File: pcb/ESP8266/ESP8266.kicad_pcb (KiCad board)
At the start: 2 copper layers, 17.5 x 27.2 mm, 18 parts, among them J1 Conn_02x04, U1 ESP8266EX, U2 W25Q16BVSSIG

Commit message: mejoras en el pcb
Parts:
- J1: footprint Connector_PinHeader_1.27mm:PinHeader_2x04_P1.27mm_Vertical -> Connector_PinHeader_2.54mm:PinHeader_2x04_P2.54mm_Vertical
- moved J1 0.79 mm to (107.0, 136.0)
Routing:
- net /RST: track 31.9 -> 18.6 mm
- net /UTXD: track 44.2 -> 32.7 mm
- net /GPIO2: track 8.27 -> 12.4 mm, vias 1 -> 2
- net /URXD: track 22.9 -> 19.3 mm
- net +3V3: track 60.6 -> 63.9 mm
- net /ENA: track 13.6 -> 12.1 mm, vias 2 -> 0
- net /GPIO0: track 5.71 -> 6.39 mm, vias 0 -> 1
- net GND: track 128.9 -> 128.4 mm

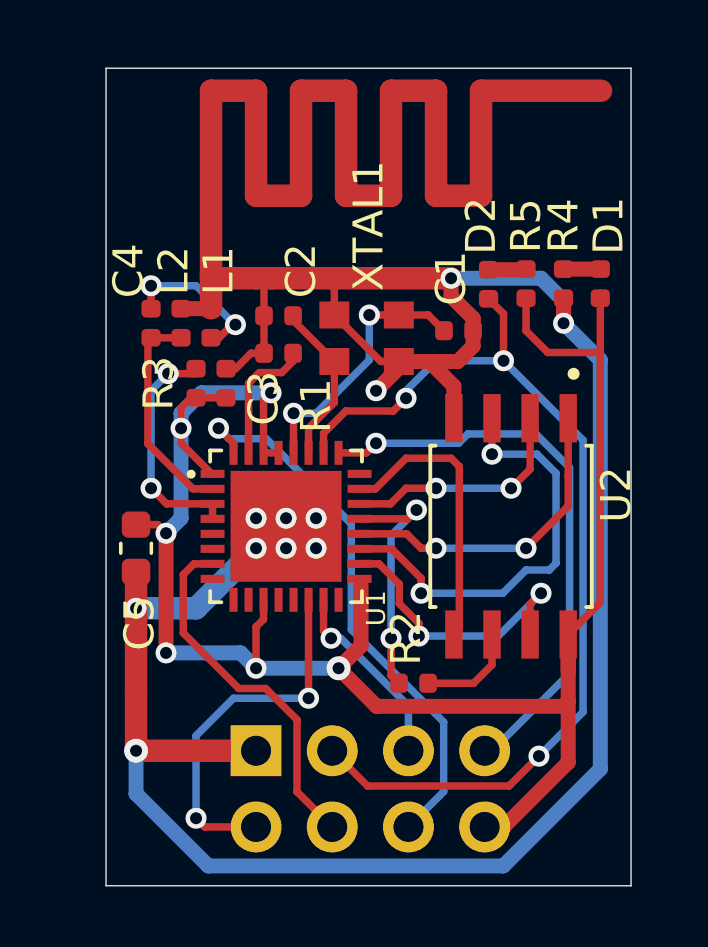
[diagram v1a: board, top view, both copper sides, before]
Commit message: agregado de modelos 3D al proeycto, fiduciales y agujero
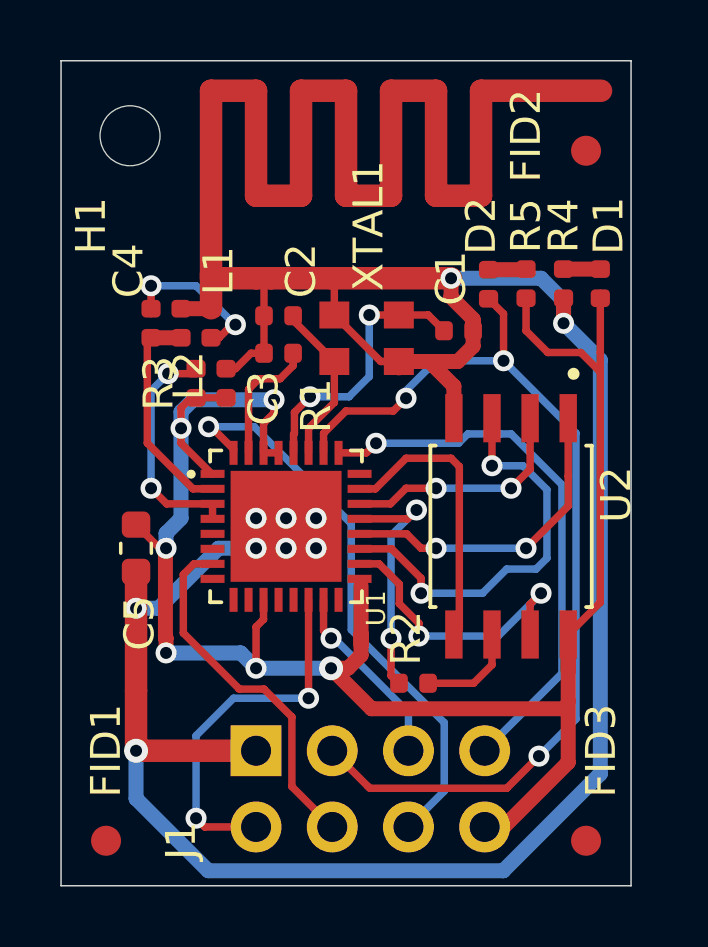
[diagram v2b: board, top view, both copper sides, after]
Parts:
- added FID1: Fiducial, Fiducial:Fiducial_1mm_Mask2mm, F.Cu at (102.0, 139.0)
- added FID2: Fiducial, Fiducial:Fiducial_1mm_Mask2mm, F.Cu at (118.0, 116.0)
- added FID3: Fiducial, Fiducial:Fiducial_1mm_Mask2mm, F.Cu at (118.0, 139.0)
- added H1: MountingHole, MountingHole:MountingHole_2mm, F.Cu at (102.8, 115.5)
- turned L2 to 270 degrees
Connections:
- L2 pad 1: Net-(C4-Pad1) -> GND
- L2 pad 2: GND -> Net-(C4-Pad1)
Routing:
- net +3V3: track 63.9 -> 65.0 mm
- net /URXD: track 19.3 -> 18.3 mm
- net Net-(U1-Pad19): track 14.5 -> 13.7 mm
- net /RST: track 18.6 -> 19.2 mm
- net GND: track 128.4 -> 128.1 mm, vias 11 -> 10
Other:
- board size 17.5 x 27.2 mm -> 19 x 27.5 mm
- net class Default: clearance 0.2 -> 0.22
- rule trace_clearance: 0.2 -> 0.22

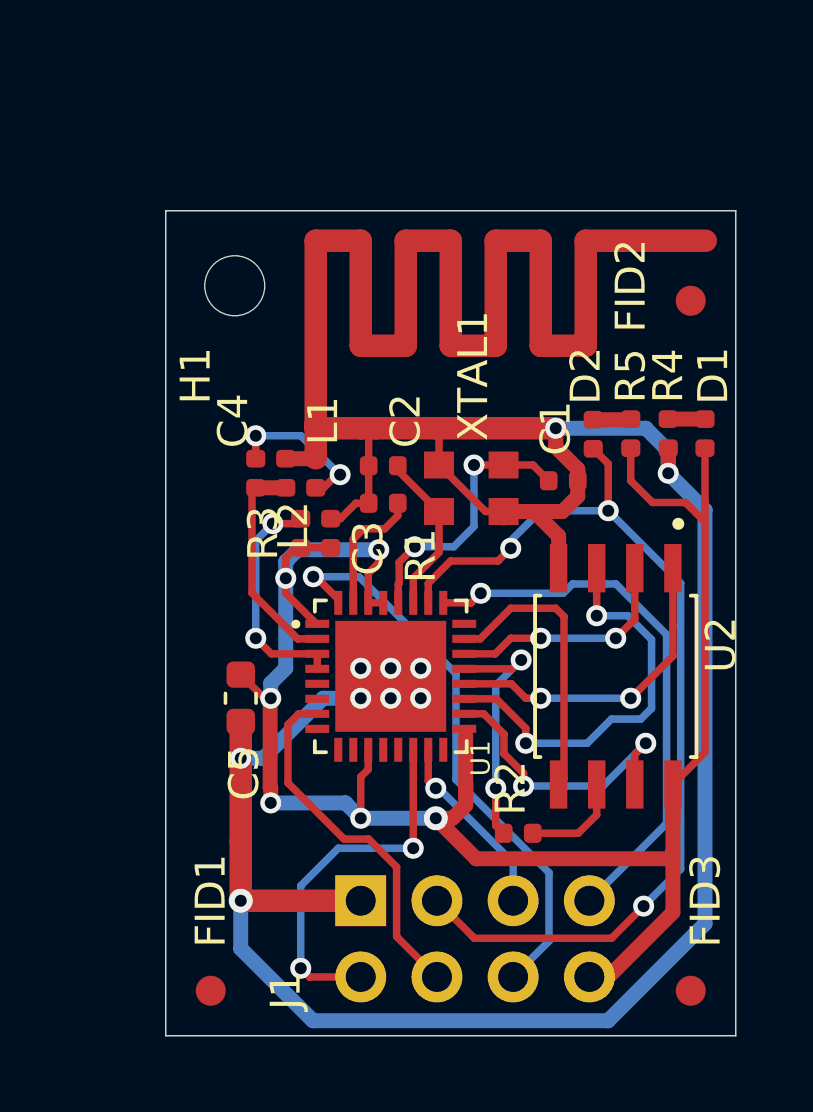
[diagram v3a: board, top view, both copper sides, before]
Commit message: board acomodado con componentes 0805
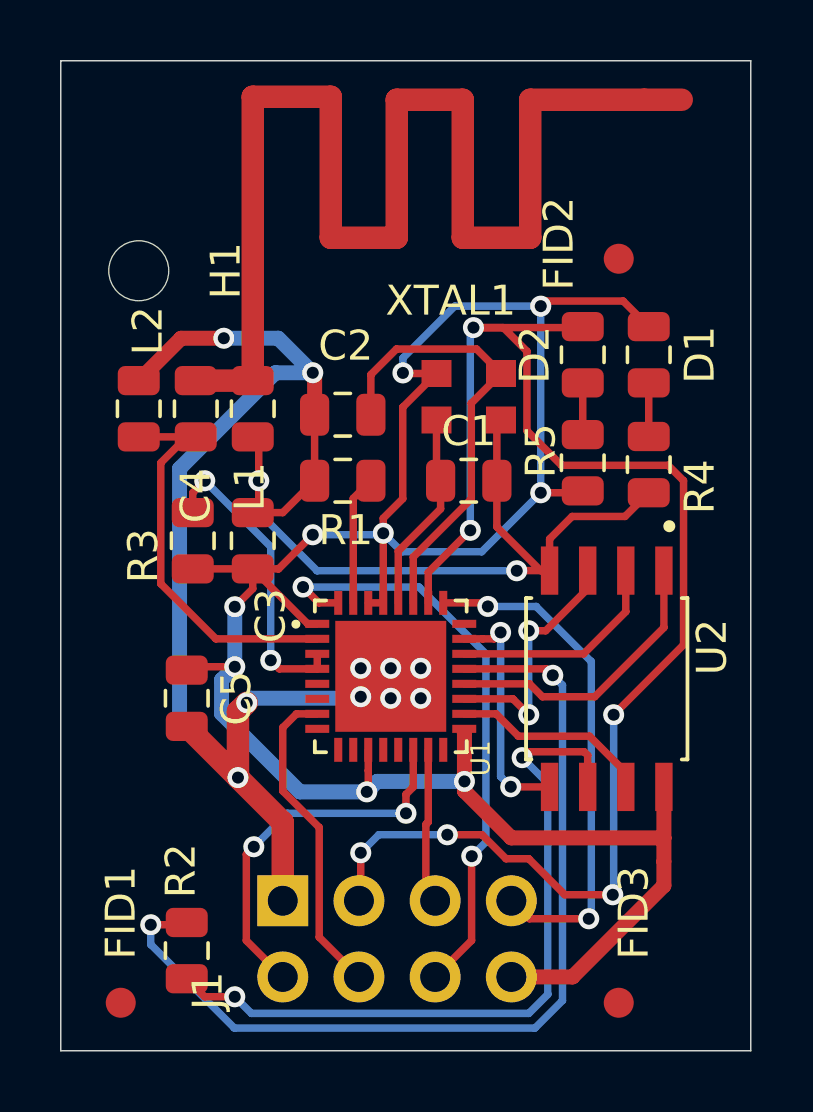
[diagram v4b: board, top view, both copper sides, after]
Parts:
- C1, C2, C3, C4: footprint Capacitor_SMD:C_0402_1005Metric -> Capacitor_SMD:C_0805_2012Metric
- C5: footprint Capacitor_SMD:C_0603_1608Metric -> Capacitor_SMD:C_0805_2012Metric
- D1, D2, R1, R2, R3, R4, R5: footprint Resistor_SMD:R_0402_1005Metric -> Resistor_SMD:R_0805_2012Metric
- L1, L2: footprint Inductor_SMD:L_0402_1005Metric -> Inductor_SMD:L_0805_2012Metric
- moved R2 11.7 mm to (101.2, 137.7), turned to 90 degrees
- moved L2 5.35 mm to (99.6, 119.6)
- moved R3 3.61 mm to (101.4, 124.0)
- moved H1 3.24 mm to (99.6, 115.0)
- moved D1 3.23 mm to (116.6, 117.8), turned to 90 degrees
- moved C1 3.15 mm to (110.6, 122.0)
- moved XTAL1 3.05 mm to (110.6, 119.2), turned to 0 degrees
- moved FID1 3.03 mm to (99.0, 139.4)
- moved L1 3.01 mm to (103.4, 119.6), turned to 90 degrees
- moved C4 2.94 mm to (101.5, 119.6)
- moved FID2 2.78 mm to (115.6, 114.6)
- moved D2 2.67 mm to (114.4, 117.8), turned to 270 degrees
- moved C3 2.61 mm to (103.4, 124.0)
- moved J1 2.60 mm to (104.4, 136.0)
- moved FID3 2.43 mm to (115.6, 139.4)
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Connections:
- XTAL1 pad 4: GND -> +3V3
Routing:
- net GND: track 128.1 -> 74.7 mm, vias 10 -> 12
- net Net-(C4-Pad2): track 5.23 -> 44.2 mm, vias 2 -> 0
- net Net-(R2-Pad2): track 8.26 -> 31.3 mm
- net Net-(R2-Pad1): track 3.39 -> 24.4 mm, vias 0 -> 2
- net /UTXD: track 32.6 -> 50.0 mm, vias 3 -> 6
- net +3V3: track 65.0 -> 80.6 mm, vias 6 -> 9
- net /SA_XTAL: track 5.50 -> 15.2 mm
- net Net-(C4-Pad1): track 7.67 -> 13.1 mm
- net Net-(U1-Pad19): track 13.7 -> 8.32 mm
- net Net-(U1-Pad18): track 9.80 -> 6.68 mm, vias 2 -> 0
- net Net-(R3-Pad2): track 7.75 -> 10.3 mm
- net /EN_XTAL: track 9.11 -> 6.74 mm, vias 2 -> 0
- net Net-(U1-Pad23): track 9.54 -> 7.88 mm, vias 0 -> 2
- net /ENA: track 12.1 -> 10.7 mm
- net /URXD: track 18.3 -> 17.2 mm, vias 1 -> 2
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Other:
- board size 19 x 27.5 mm -> 23 x 33 mm
- net class Default: clearance 0.22 -> 0.24
- rule trace_clearance: 0.22 -> 0.24

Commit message: agregado de comentarios
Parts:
- moved FID3 53.4 mm to (157.0, 105.6)
- moved FID2 53.4 mm to (157.0, 80.8)
- moved U1 52.3 mm to (148.0, 94.8)
- moved C1 52.3 mm to (150.6, 88.2)
- moved C2 52.3 mm to (146.4, 86.0)
- moved C3 52.3 mm to (143.4, 90.2)
- moved C4 52.3 mm to (141.5, 85.8)
- moved D1 52.3 mm to (156.6, 84.0)
- moved D2 52.3 mm to (154.4, 84.0)
- moved FID1 52.3 mm to (139.0, 105.7)
- moved H1 52.3 mm to (139.6, 81.2)
- moved J1 52.3 mm to (144.4, 102.2)
- moved L1 52.3 mm to (143.4, 85.8)
- moved L2 52.3 mm to (139.6, 85.8)
- moved R1 52.3 mm to (146.4, 88.2)
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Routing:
- net Net-(C4-Pad2): track 44.2 -> 54.6 mm
- net /UTXD: track 50.0 -> 51.7 mm
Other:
- board text added: "* No se tiene restricciones sobre el tamaño de pistas. * Se utilizo las capacidades de fabricación nacional (Mayer). * La capacidad de Mayer planteada para este módulo fue 10 mils * La grilla utilizada para acomodar componente cómo primera aproximación fue 1mm * La grilla utilizada para routear las pistas varió entre 0.25 a 0.1mm"
- board text added: "ESP01 Rev 1.1 Ind Arg"

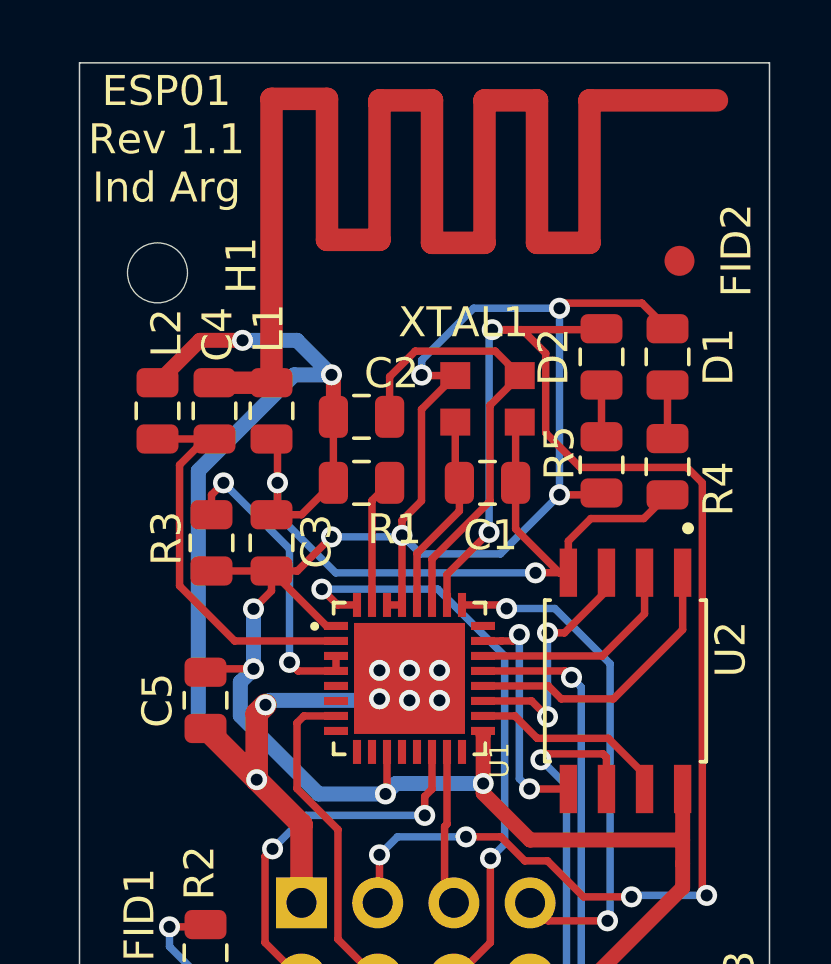
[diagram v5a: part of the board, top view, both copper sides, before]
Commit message: agregados componentes digikey
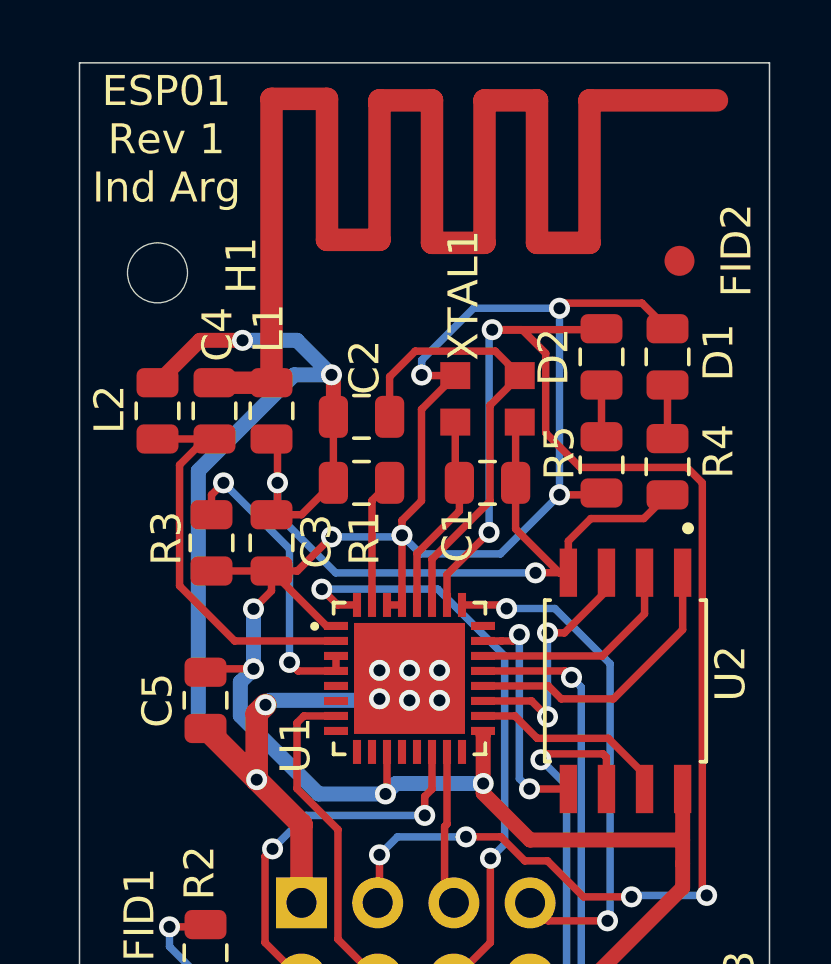
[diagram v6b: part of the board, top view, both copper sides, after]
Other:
- board text added: "ESP01 Rev 1 Ind Arg"
- board text removed: "ESP01 Rev 1.1 Ind Arg"

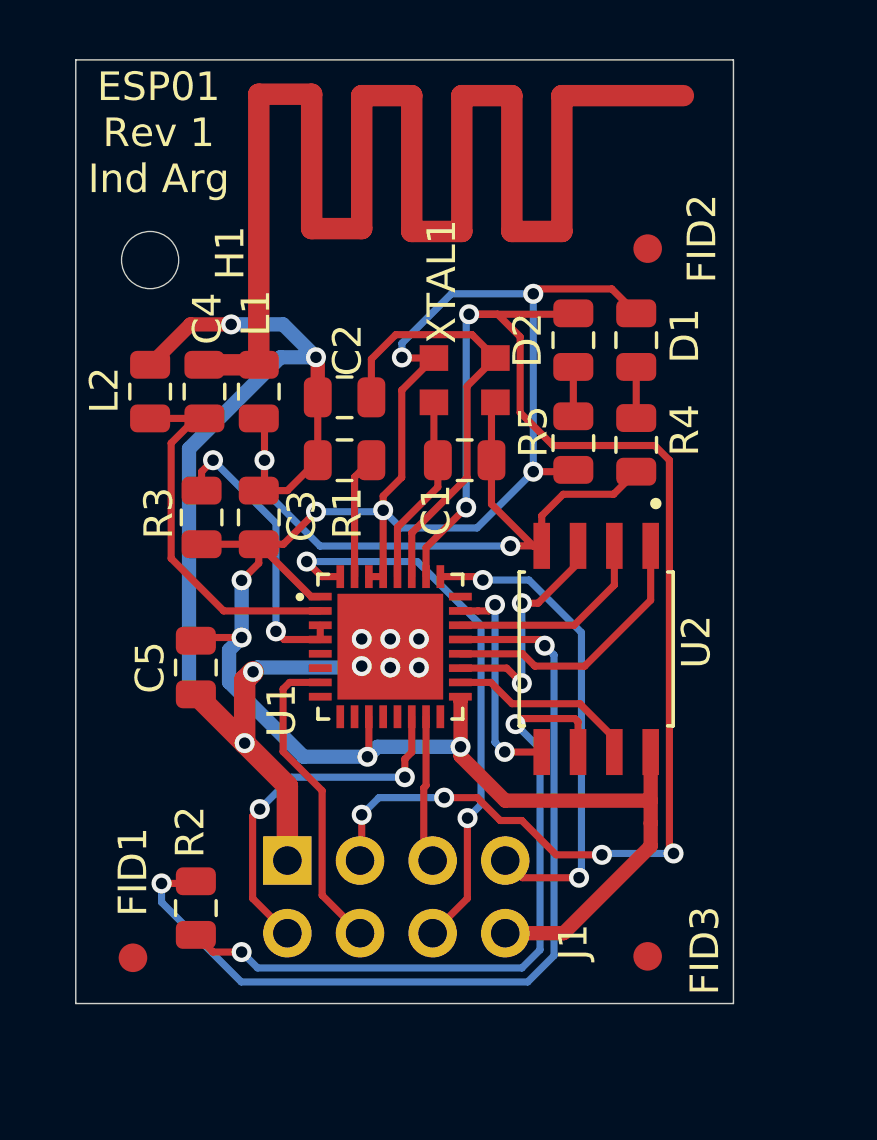
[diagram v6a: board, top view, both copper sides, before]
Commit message: agregado de logos y e informacion para fabricacion
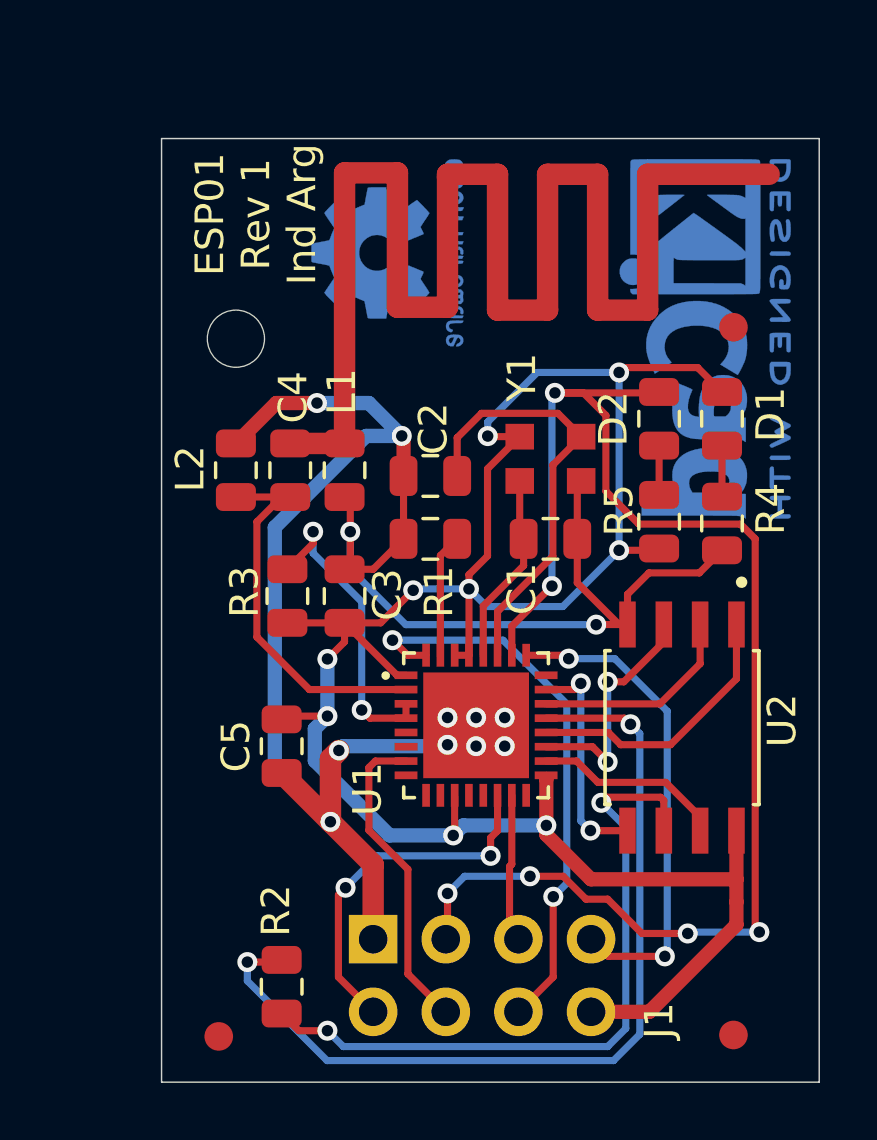
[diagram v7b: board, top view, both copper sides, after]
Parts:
- added LOGO1: Logo_Open_Hardware_Small, Symbol:KiCad-Logo2_5mm_Copper, B.Cu at (159.0, 84.0)
- added LOGO2: Logo_Open_Hardware_Small, Symbol:OSHW-Logo2_7.3x6mm_Copper, B.Cu at (148.0, 81.0)
- moved C1 4.07 mm to (153.6, 91.0)
- moved C2 4.07 mm to (149.4, 88.8)
- moved C3 4.07 mm to (146.4, 93.0)
- moved C4 4.07 mm to (144.5, 88.6)
- moved C5 4.07 mm to (144.2, 98.2)
- moved D1 4.07 mm to (159.6, 86.8)
- moved D2 4.07 mm to (157.4, 86.8)
- moved FID1 4.07 mm to (142.0, 108.4)
- moved FID2 4.07 mm to (160.0, 83.6)
- moved FID3 4.07 mm to (160.0, 108.3)
- moved H1 4.07 mm to (142.6, 84.0)
- moved J1 4.07 mm to (147.4, 105.0)
- moved L1 4.07 mm to (146.4, 88.6)
- moved L2 4.07 mm to (142.6, 88.6)
- moved R1 4.07 mm to (149.4, 91.0)
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- renumbered XTAL1 to Y1
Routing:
- net Net-(R3-Pad2): track 10.3 -> 10.8 mm
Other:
- board text added: "Board dimension: 23x33 mm 2 Layers - thickness: 1.6 mm Surface finish: HASL with lead Grid: 0.1mm Clearance: 0.24 mm Track Width: 0.25mm Via size: 0.7mm Via Drill: 0.4mm Tented Vias Reference specs: MAYER pcb"
- board text removed: "* No se tiene restricciones sobre el tamaño de pistas. * Se utilizo las capacidades de fabricación nacional (Mayer). * La capacidad de Mayer planteada para este módulo fue 10 mils * La grilla utilizada para acomodar componente cómo primera aproximación fue 1mm * La grilla utilizada para routear las pistas varió entre 0.25 a 0.1mm"
